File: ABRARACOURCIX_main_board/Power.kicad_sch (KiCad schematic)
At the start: 2 parts, among them U3 AZ1117CH-3.3TRG1, U4 LT1529CQ-5_PBF

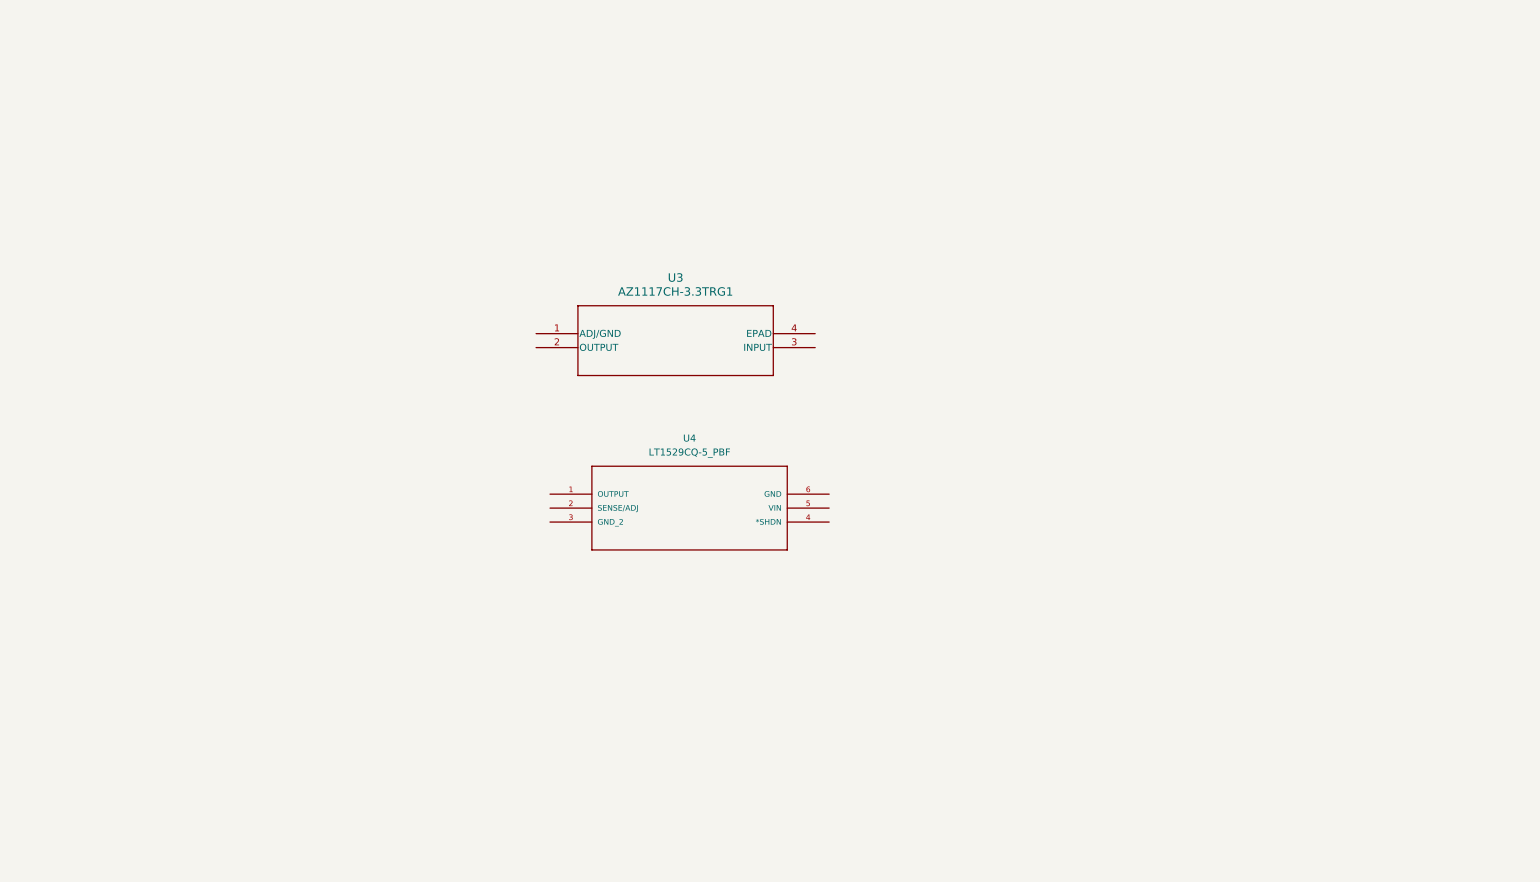
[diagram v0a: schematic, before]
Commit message: Terminé les interconnects
Toutes les interfaces et le power sont terminés. (À vérifier)
Reste à ajouter toutes les connexions au ICM et stm32
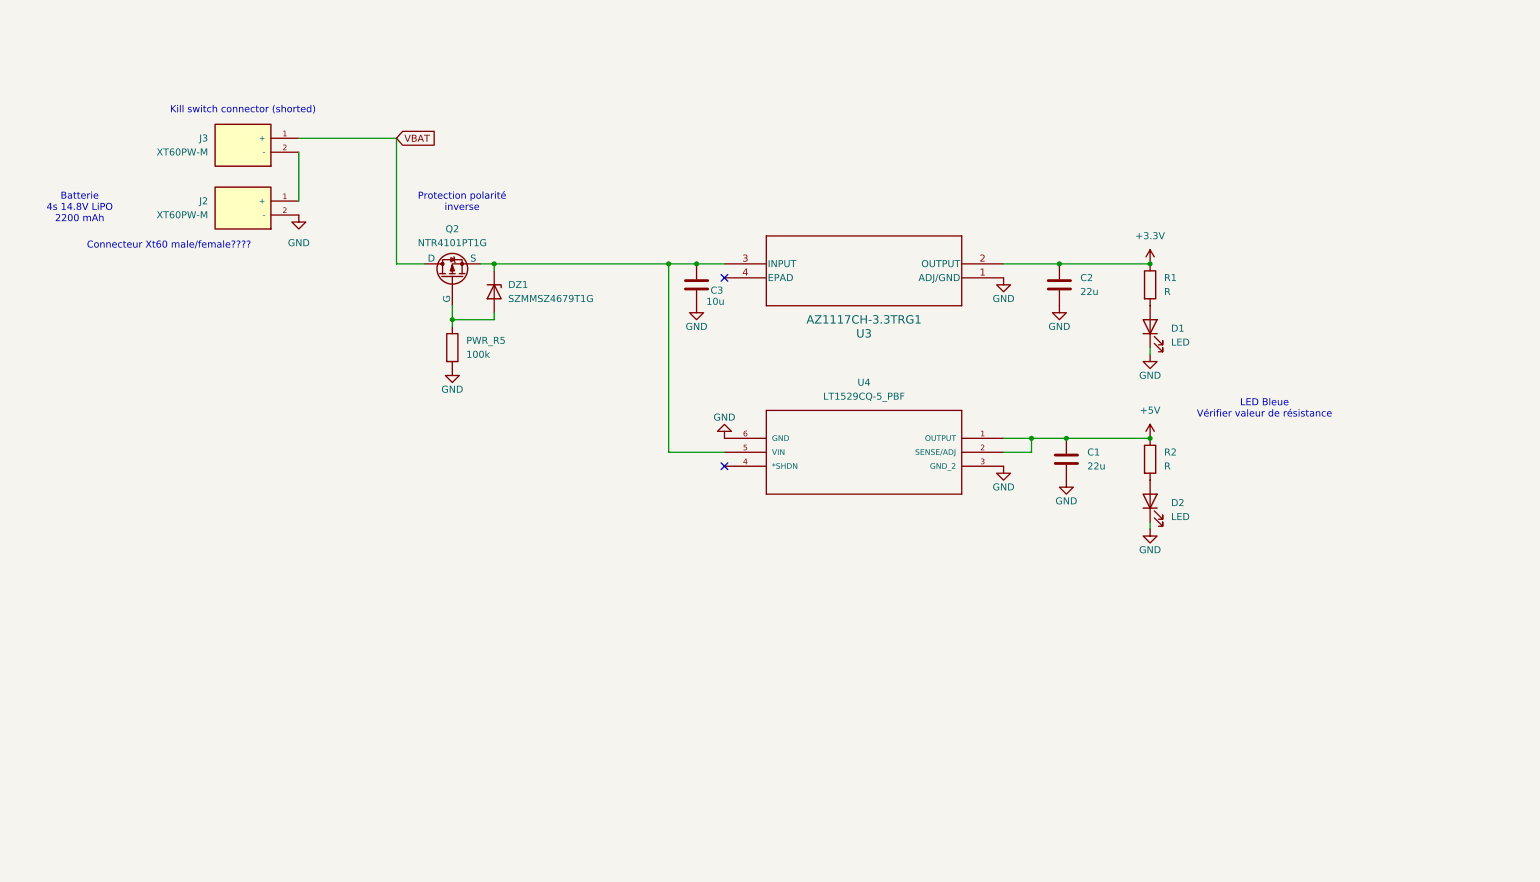
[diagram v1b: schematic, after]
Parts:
- added C1, C2: 22u, symbol Device:C
- added C3: 10u, symbol Device:C
- added D1, D2: LED, symbol Device:LED
- added DZ1: SZMMSZ4679T1G, Diode_SMD:D_SOD-123, symbol Diode:BZV55C18
- added J2, J3: XT60PW-M, XT60PW-M:AMASS_XT60PW-M, symbol GAUL_ABRARACOURCIX:XT60PW-M
- added PWR_R5: 100k, Resistor_SMD:R_1206_3216Metric, symbol Device:R
- added Q2: NTR4101PT1G, Footprints:SOT-23, symbol Simulation_SPICE:PMOS
- added R1, R2: R, symbol Device:R
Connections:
- net +5V: now reaches U4.1 (OUTPUT)
- net +5V: now also U4.2 (SENSE/ADJ), C1.1, R2.1
- net GND: now reaches U4.3 (GND_2)
- net GND: now also U3.1 (ADJ/GND), U4.6 (GND), C1.2, C2.2, C3.2, D1.1 (K), D2.1 (K), J2.2 (-), PWR_R5.2
- net at U4.5 (VIN): now also U3.3 (INPUT), C3.1, DZ1.1 (K), Q2.3 (S)
- net +3.3V: now reaches U3.2 (OUTPUT)
- net +3.3V: now also C2.1, R1.1
- new net: J2.1 (+), J3.2 (-)
- new net: D2.2 (A), R2.2
- new net: DZ1.2 (A), PWR_R5.1, Q2.2 (G)
- new net: D1.2 (A), R1.2
- new net VBAT: J3.1 (+), Q2.1 (D)
- no-connect marks 0 -> 2
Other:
- note added: "Batterie 4s 14.8V LiPO 2200 mAh"
- note added: "Connecteur Xt60 male/female????"
- note added: "Kill switch connector (shorted)"
- note added: "LED Bleue Vérifier valeur de résistance"
- note added: "Protection polarité inverse"
- moved on the sheet: U3, U4

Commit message: Reprise de contrôle
Schematics terminés
Reste à associer des composantes et vérification
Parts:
- removed D2: LED, symbol Device:LED
- removed J2: XT60PW-M, XT60PW-M:AMASS_XT60PW-M, symbol GAUL_ABRARACOURCIX:XT60PW-M
- removed R2: R, symbol Device:R
- removed U4: LT1529CQ-5_PBF, LT1529CQ-5_PBF:DDPAK-5_Q, symbol GAUL_ABRARACOURCIX:LT1529CQ-5_PBF
- added C28: 1n, symbol Device:C
- added C29: 0.1u, symbol Device:C
- added R3: 1k, symbol Device:R
- added R4: 2k, symbol Device:R
- added R8: 50k, symbol Device:R
- added R9: 10k, symbol Device:R
- added SW1: Motor, symbol Switch:SW_SPST
- added SW2: Master, symbol Switch:SW_SPST
- added U2: Current_sens_ACS712ELCTR-20A-T, ACS712ELCTR-20A-T:SOIC127P600X175-8N, symbol GAUL_ABRARACOURCIX:Current_sens_ACS712ELCTR-20A-T
- added U4: Xl4015, symbol GAUL_ABRARACOURCIX:Buck_Xl4015_breakout
- added U6: OP1177ARM, Package_SO:MSOP-8_3x3mm_P0.65mm, symbol Amplifier_Operational:OP1177ARM
- D1: value LED -> 599-0410-127F; Digikey (none) -> https://www.digikey.ca/en/products/detail/dialight/599-0410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
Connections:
- net +3.3V: now also U6.7 (V+)
- net +5V: now also C29.1, U2.8 (VCC), U4. (Out-)
- net GND: now also J3.2 (-), C28.2, C29.2, R4.2, R9.2, U2.5 (GND), U4. (Out-), U6.4 (V-)
- net VBAT: now also SW1.2 (B); no longer J3.1 (+), Q2.1 (D)
- net at C3.1, DZ1.1 (K), Q2.3 (S)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: now also U4. (Out-)
- new net: R8.2, R9.1, U6.3 (+)
- new net: J3.1 (+), SW2.1 (A)
- new net: R3.1, U2.7 (VIOUT)
- new net: Q2.1 (D), SW1.1 (A), U2.3 (IP-__1), U2.4 (IP-)
- new net: C28.1, U2.6 (FILTER)
- new net VBAT_ADC: U6.2 (-), U6.6
- new net VBAT_sense: R8.1, SW2.2 (B), U2.1 (IP+), U2.2 (IP+__1)
- new net VIout_sense: R3.2, R4.1
- no-connect marks 2 -> 1
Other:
- note added: "Breakout board ajustable Remplacer les potentiomètres par resistance appropriées 5A absolute max"
- note added: "Connecteur Xt60 male"
- note added: "LED rouge VLED = 2.1V à 30 mA R= (3.3-2.1)/30mA = 40 Ohm"
- note added: "Max 20A DC"
- note added: "Ratio minimum de 4.1 entre R8 et R9"
- note added: "Vérifier la robustesse avec une mauvaise séquence de power up et power down"
- note added: "À changer l'OP Amp (circuit différentiel?)"
- note removed: "Connecteur Xt60 male/female????"
- note removed: "Kill switch connector (shorted)"
- note removed: "LED Bleue Vérifier valeur de résistance"
- moved on the sheet: C1, C2, C3, D1, DZ1, J3, PWR_R5, Q2, R1, U3

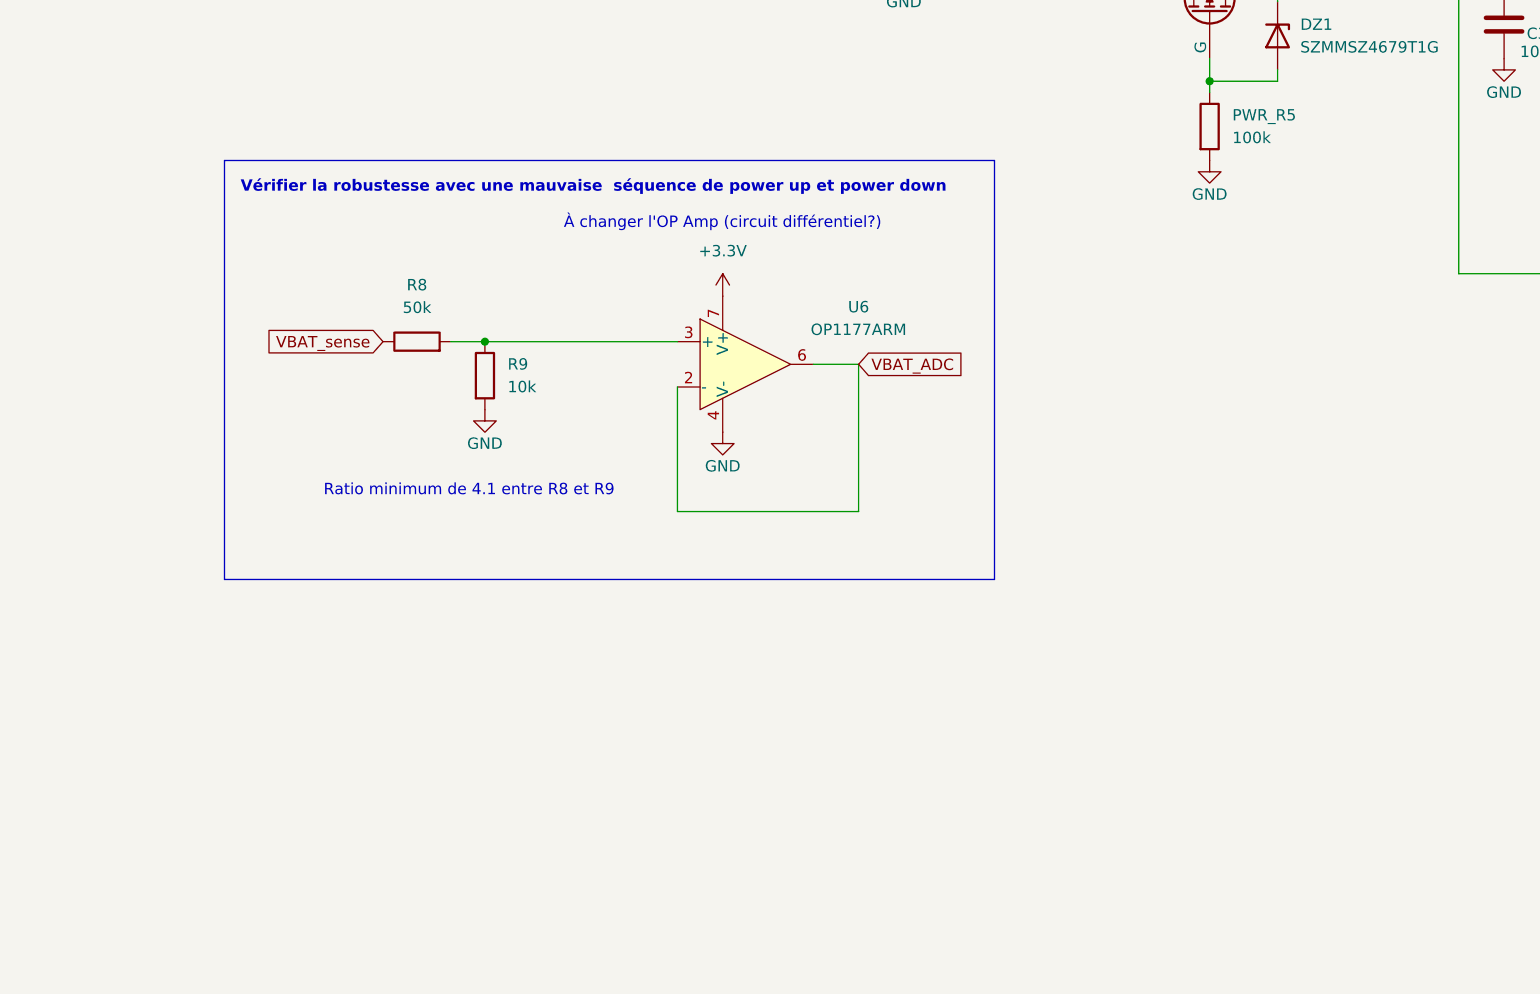
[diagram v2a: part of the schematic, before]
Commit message: Modif lecture tension
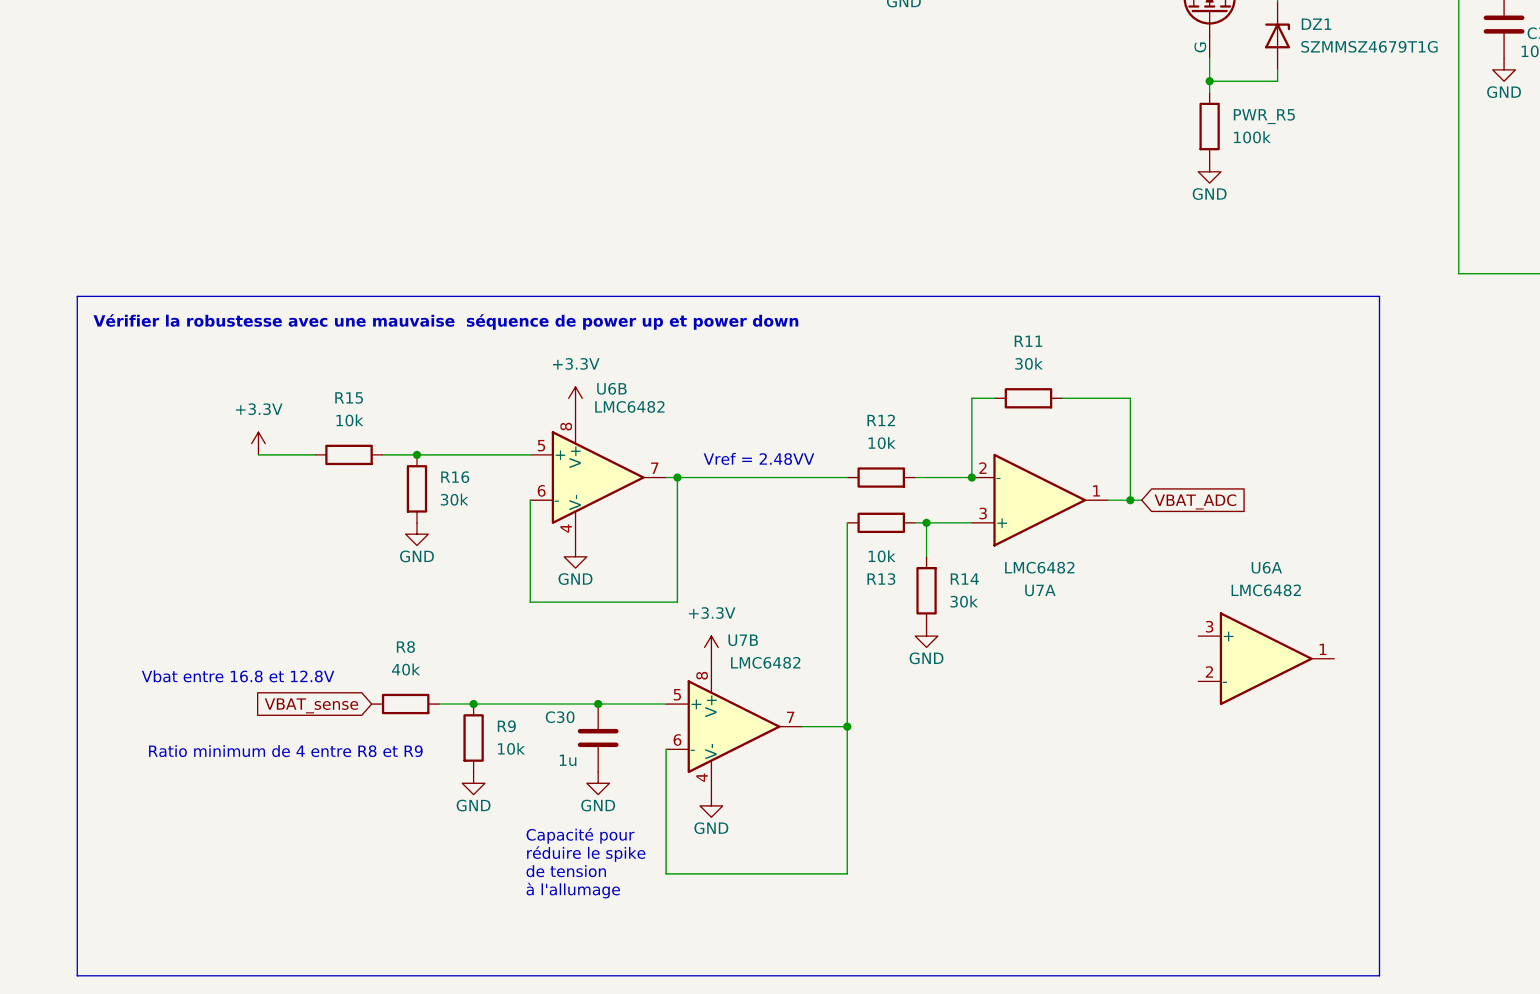
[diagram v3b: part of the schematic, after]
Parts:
- removed U6: OP1177ARM, Package_SO:MSOP-8_3x3mm_P0.65mm, symbol Amplifier_Operational:OP1177ARM
- added C30: 1u, symbol Device:C
- added R11, R14, R16: 30k, symbol Device:R
- added R12, R13, R15: 10k, symbol Device:R
- added U6, U7: LMC6482, symbol Amplifier_Operational:LMC6482
- R8: value 50k -> 40k
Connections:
- net +3.3V: now also R15.1, U6.8 (V+), U7.8 (V+)
- net GND: now also C30.2, R14.1, R16.2, U6.4 (V-), U7.4 (V-)
- net VBAT_ADC: now also R11.2, U7.1
- net at R8.2, R9.1: now also C30.1, U7.5 (+)
- new net: R11.1, R12.2, U7.2 (-)
- new net: R13.2, R14.2, U7.3 (+)
- new net: R15.2, R16.1, U6.5 (+)
- new net: R13.1, U7.6 (-), U7.7
- new net: R12.1, U6.6 (-), U6.7
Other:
- note added: "Capacité pour réduire le spike de tension à l'allumage"
- note added: "Ratio minimum de 4 entre R8 et R9"
- note added: "Vbat entre 16.8 et 12.8V"
- note added: "Vref = 2.48VV"
- note removed: "Ratio minimum de 4.1 entre R8 et R9"
- note removed: "À changer l'OP Amp (circuit différentiel?)"
- moved on the sheet: R8, R9
